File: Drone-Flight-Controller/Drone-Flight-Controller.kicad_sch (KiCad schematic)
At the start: 57 parts, among them J1 Screw_Terminal_01x02, J10 TestPoint, J11 TestPoint, J12 TestPoint, J2 Raspberry_Pi_4, J3 TestPoint, J4 TestPoint, J5 TestPoint, J6 TestPoint, J7 TestPoint, J8 TestPoint, J9 TestPoint, Q1 BSS138, Q2 BSS138, Q3 BSS138, Q4 BSS138, SW1 SW_Omron_B3FS, U1 MCP1700x-180xxMB, U2 LMR51430, U3 ADC101C021CIMK, U4 ICM-20948, U5 BMP280, U6 PCA9531PW

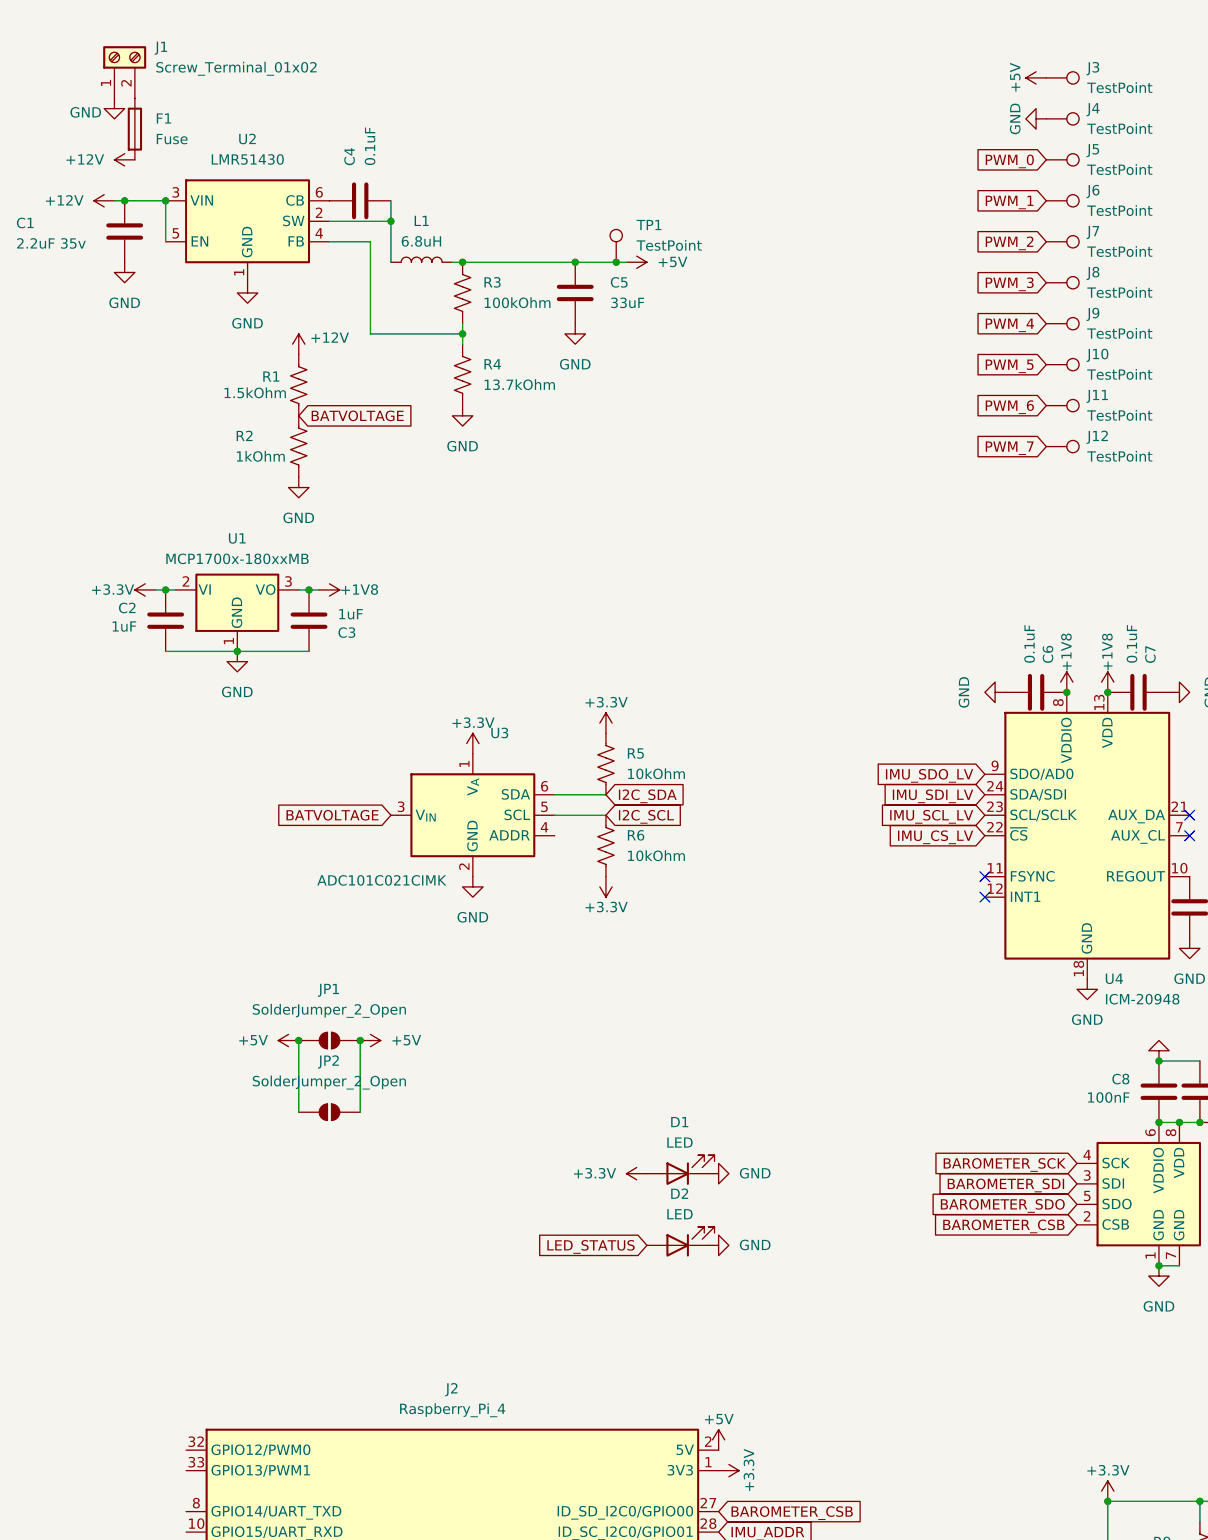
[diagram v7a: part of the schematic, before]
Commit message: optimized routing
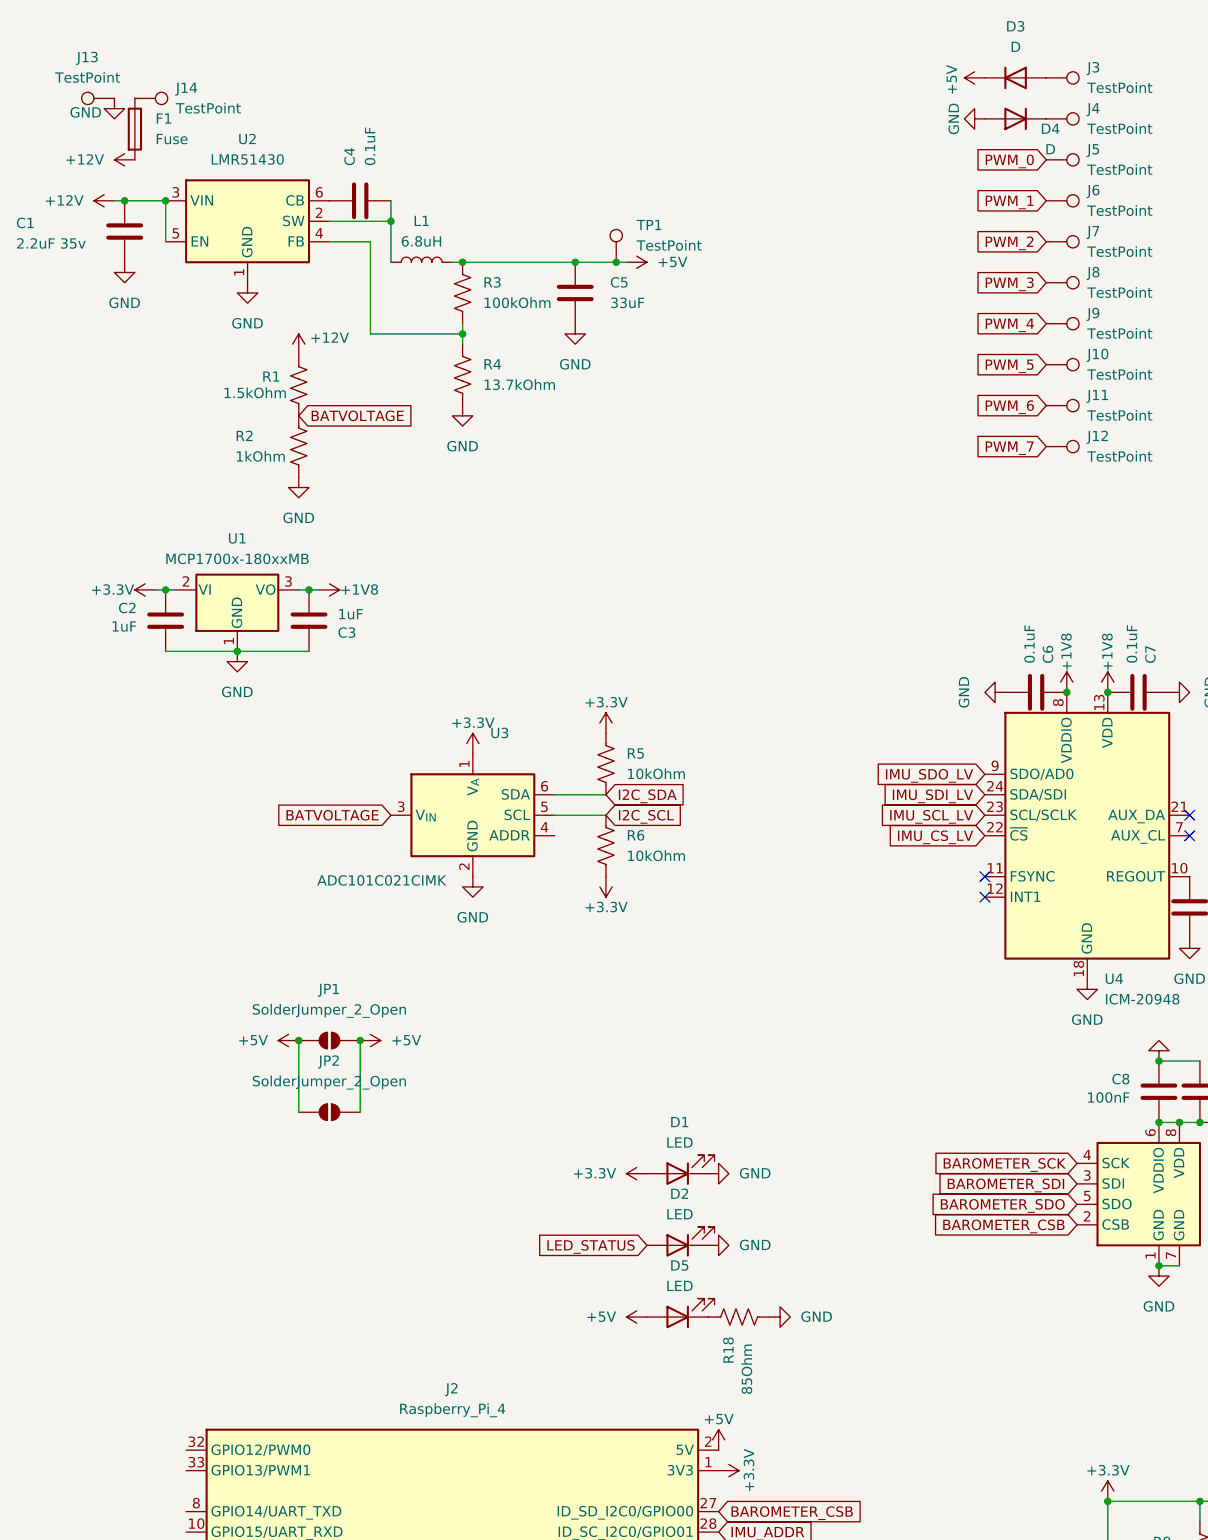
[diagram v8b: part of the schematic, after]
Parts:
- removed J1: Screw_Terminal_01x02, TerminalBlock:TerminalBlock_Xinya_XY308-2.54-2P_1x02_P2.54mm_Horizontal, symbol Connector:Screw_Terminal_01x02
- added D3, D4: D, Diode_SMD:D_0805_2012Metric, symbol Device:D
- added D5: LED, LED_SMD:LED_0402_1005Metric, symbol Device:LED
- added J13, J14: TestPoint, TestPoint:TestPoint_Pad_D2.0mm, symbol Connector:TestPoint
- added R18: 85Ohm, Resistor_SMD:R_0402_1005Metric, symbol Device:R_US
- SW1: footprint Button_Switch_SMD:SW_SPST_Omron_B3FS-100xP -> Button_Switch_SMD:SW_Push_1P1T_NO_CK_KMR2
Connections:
- net +5V: now also D3.1 (K), D5.2 (A); no longer J3.1
- net GND: now also D4.2 (A), J13.1, R18.2; no longer J4.1
- net at F1.1: now also J14.1
- new net: D5.1 (K), R18.1
- new net: D3.2 (A), J3.1
- new net: D4.1 (K), J4.1
